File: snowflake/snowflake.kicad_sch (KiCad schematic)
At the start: 19 parts, among them SW1 SK-12E12-G040, U1 RGB, U2 RGB, U25 TPS61022, U3 RGB, U4 RGB

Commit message: 2/6 branches
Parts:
- added C10, C11, C12, C13, C14, C15, C16, C17, C18, C19, C20, C21, C22, C23, C24, C5, C6, C7, C8, C9: 100nF, C_0603_1608Metric, symbol Device:C
- added U10, U11, U12, U13, U14, U15, U16, U17, U18, U19, U20, U21, U22, U23, U24, U5, U6, U7, U8, U9: RGB, easyeda2kicad:LED-SMD_4P-L5.0-W5.0-TL_WS2812B-B, symbol easyeda2kicad:TZ-5050S2RGB-5V-I4-H1
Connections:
- net +5V: now also C10.2, C11.2, C12.2, C13.2, C14.2, C15.2, C16.2, C17.2, C18.2, C19.2, C20.2, C21.2, C22.2, C23.2, C24.2, C5.2, C6.2, C7.2, C8.2, C9.2, U10.1 (VDD), U11.1 (VDD), U12.1 (VDD), U13.1 (VDD), U14.1 (VDD), U15.1 (VDD), U16.1 (VDD), U17.1 (VDD), U18.1 (VDD), U19.1 (VDD), U20.1 (VDD), U21.1 (VDD), U22.1 (VDD), U23.1 (VDD), U24.1 (VDD), U5.1 (VDD), U6.1 (VDD), U7.1 (VDD), U8.1 (VDD), U9.1 (VDD)
- net GND: now also C10.1, C11.1, C12.1, C13.1, C14.1, C15.1, C16.1, C17.1, C18.1, C19.1, C20.1, C21.1, C22.1, C23.1, C24.1, C5.1, C6.1, C7.1, C8.1, C9.1, U10.3 (GND), U11.3 (GND), U12.3 (GND), U13.3 (GND), U14.3 (GND), U15.3 (GND), U16.3 (GND), U17.3 (GND), U18.3 (GND), U19.3 (GND), U20.3 (GND), U21.3 (GND), U22.3 (GND), U23.3 (GND), U24.3 (GND), U5.3 (GND), U6.3 (GND), U7.3 (GND), U8.3 (GND), U9.3 (GND)
- net at U4.2 (DOU): now also U5.4 (DIN)
- new net: U5.2 (DOU), U6.4 (DIN)
- new net: U15.2 (DOU), U16.4 (DIN)
- new net: U14.2 (DOU), U15.4 (DIN)
- new net: U10.4 (DIN), U9.2 (DOU)
- new net: U8.2 (DOU), U9.4 (DIN)
- new net: U22.2 (DOU), U23.4 (DIN)
- new net: U21.2 (DOU), U22.4 (DIN)
- new net: U11.2 (DOU), U12.4 (DIN)
- new net: U10.2 (DOU), U11.4 (DIN)
- new net: U18.2 (DOU), U19.4 (DIN)
- new net: U17.2 (DOU), U18.4 (DIN)
- new net: U23.2 (DOU), U24.4 (DIN)
- new net: U7.2 (DOU), U8.4 (DIN)
- new net: U16.2 (DOU), U17.4 (DIN)
- new net: U13.2 (DOU), U14.4 (DIN)
- new net: U12.2 (DOU), U13.4 (DIN)
- new net: U19.2 (DOU), U20.4 (DIN)
- new net: U6.2 (DOU), U7.4 (DIN)
- new net: U20.2 (DOU), U21.4 (DIN)

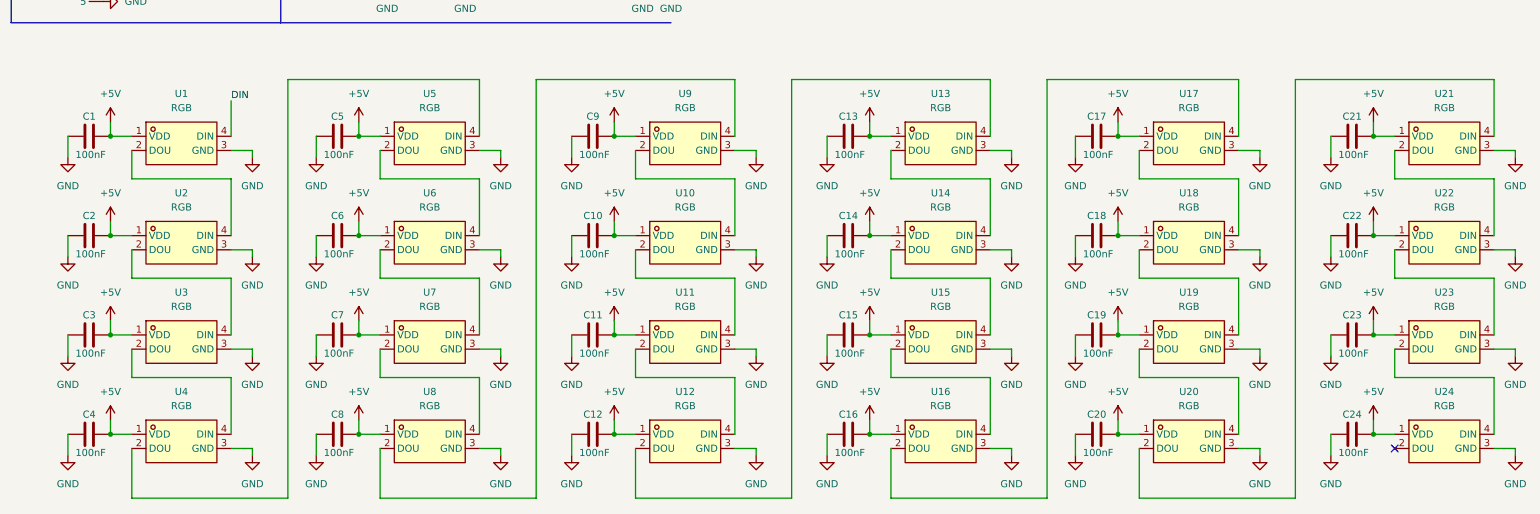
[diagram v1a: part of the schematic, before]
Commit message: Add JLCPCB Part Numbers
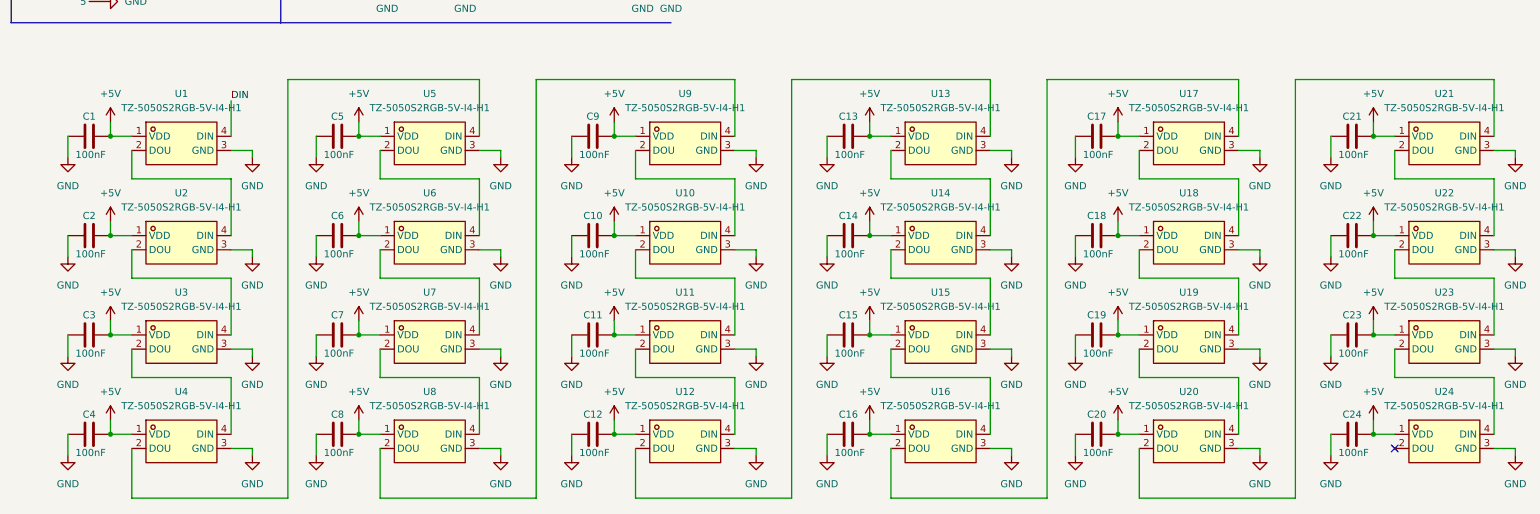
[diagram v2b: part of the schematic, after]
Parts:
- C0: LCSC Part (none) -> C36911391
- C1, C10, C11, C12, C13, C14, C15, C16, C17, C18, C19, C2, C20, C21, C22, C23, C24, C3, C4, C5, C6, C7, C8, C9: footprint C_0603_1608Metric -> Capacitor_SMD:C_0603_1608Metric; LCSC Part (none) -> C36911391
- C25, C26: LCSC Part (none) -> C20416425
- C27: LCSC Part (none) -> C6119842
- R1: LCSC Part (none) -> C5159692
- R2: LCSC Part (none) -> C49652939
- U1, U10, U11, U12, U13, U14, U15, U16, U17, U18, U19, U2, U20, U21, U22, U23, U24, U3, U4, U5, U6, U7, U8, U9: value RGB -> TZ-5050S2RGB-5V-I4-H1
- U25: LCSC Part (none) -> C915088

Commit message: Submitted for cost estimate from JLCPCB
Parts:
- BAT1: LCSC (none) -> C254917; LCSC Part C254917 -> (none)
- C0, C1, C10, C11, C12, C13, C14, C15, C16, C17, C18, C19, C2, C20, C21, C22, C23, C24, C3, C4, C5, C6, C7, C8, C9: LCSC (none) -> C36911391; LCSC Part C36911391 -> (none)
- C25, C26: LCSC (none) -> C20416425; LCSC Part C20416425 -> (none)
- C27: LCSC (none) -> C6119842; LCSC Part C6119842 -> (none)
- L1: LCSC (none) -> C5179444; LCSC Part C5179444 -> (none)
- MCU1: LCSC (none) -> C5346354; LCSC Part C5346354 -> (none)
- R1: LCSC (none) -> C5159692; LCSC Part C5159692 -> (none)
- R2: LCSC (none) -> C49652939; LCSC Part C49652939 -> (none)
- SW1: LCSC (none) -> C22448007; LCSC Part C22448007 -> (none)
- U1, U10, U11, U12, U13, U14, U15, U16, U17, U18, U19, U2, U20, U21, U22, U23, U24, U3, U4, U5, U6, U7, U8, U9: LCSC (none) -> C26167850; LCSC Part C26167850 -> (none)
- U25: LCSC (none) -> C915088; LCSC Part C915088 -> (none)
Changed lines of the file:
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@@
 			)
 		)
-		(property "LCSC Part" "C6119842"
+		(property "LCSC" "C6119842"
 			(at 78.74 21.59 90)
 			(effects
@@
 			)
 		)
-		(property "LCSC Part" "C36911391"
+		(property "LCSC" "C36911391"
 			(at 116.84 120.65 90)
 			(effects
@@
 			)
 		)
-		(property "LCSC Part" "C254917"
-			(at 50.8 48.26 0)
+		(property "LCSC" "C254917"
+			(at 50.8 36.83 0)
 			(effects
 				(font
@@
 			)
 		)
-		(property "LCSC Part" "C36911391"
+		(property "LCSC" "C36911391"
 			(at 162.56 102.87 90)
 			(effects
@@
 			)
 		)
-		(property "LCSC Part" "C26167850"
-			(at 87.63 80.01 0)
+		(property "LCSC" "C26167850"
+			(at 87.63 68.58 0)
 			(effects
 				(font
@@
 			)
 		)
-		(property "LCSC Part" "C36911391"
+		(property "LCSC" "C36911391"
 			(at 116.84 102.87 90)
 			(effects
@@
 			)
 		)
-		(property "LCSC Part" "C36911391"
+		(property "LCSC" "C36911391"
 			(at 26.67 85.09 90)
 			(effects
@@
 			)
 		)
-		(property "LCSC Part" "C36911391"
+		(property "LCSC" "C36911391"
 			(at 252.73 102.87 90)
 			(effects
@@
 			)
 		)
-		(property "LCSC Part" "C5346354"
-			(at 60.96 176.53 0)
+		(property "LCSC" "C5346354"
+			(at 60.96 162.56 0)
 			(effects
 				(font
@@
 			)
 		)
-		(property "LCSC Part" "C915088"
+		(property "LCSC" "C915088"
 			(at 93.98 31.75 0)
 			(effects
@@
 			)
 		)
-		(property "LCSC Part" "C36911391"
+		(property "LCSC" "C36911391"
 			(at 26.67 120.65 90)
 			(effects
@@
 			)
 		)
-		(property "LCSC Part" "C26167850"
-			(at 179.07 115.57 0)
+		(property "LCSC" "C26167850"
+			(at 179.07 104.14 0)
 			(effects
 				(font
@@
 			)
 		)
-		(property "LCSC Part" "C36911391"
+		(property "LCSC" "C36911391"
 			(at 252.73 85.09 90)
 			(effects
@@
 			)
 		)
-		(property "LCSC Part" "C36911391"
+		(property "LCSC" "C36911391"
 			(at 71.12 85.09 90)
 			(effects
@@
 			)
 		)
-		(property "LCSC Part" "C36911391"
+		(property "LCSC" "C36911391"
 			(at 207.01 120.65 90)
 			(effects
@@
 			)
 		)
-		(property "LCSC Part" "C36911391"
+		(property "LCSC" "C36911391"
 			(at 252.73 120.65 90)
 			(effects
@@
 			)
 		)
-		(property "LCSC Part" "C26167850"
-			(at 133.35 80.01 0)
+		(property "LCSC" "C26167850"
+			(at 133.35 68.58 0)
 			(effects
 				(font
@@
 			)
 		)
-		(property "LCSC Part" "C36911391"
+		(property "LCSC" "C36911391"
 			(at 162.56 67.31 90)
 			(effects
@@
 			)
 		)
-		(property "LCSC Part" "C5159692"
+		(property "LCSC" "C5159692"
 			(at 113.03 31.75 90)
 			(effects
@@
 			)
 		)
-		(property "LCSC Part" "C36911391"
+		(property "LCSC" "C36911391"
 			(at 26.67 67.31 90)
 			(effects
@@
 			)
 		)
-		(property "LCSC Part" "C26167850"
-			(at 269.24 97.79 0)
+		(property "LCSC" "C26167850"
+			(at 269.24 86.36 0)
 			(effects
 				(font
@@
 			)
 		)
-		(property "LCSC Part" "C26167850"
-			(at 43.18 97.79 0)
+		(property "LCSC" "C26167850"
+			(at 43.18 86.36 0)
 			(effects
 				(font
@@
 			)
 		)
-		(property "LCSC Part" "C49652939"
+		(property "LCSC" "C49652939"
 			(at 120.65 31.75 90)
 			(effects
@@
 			)
 		)
-		(property "LCSC Part" "C36911391"
+		(property "LCSC" "C36911391"
 			(at 162.56 120.65 90)
 			(effects
@@
 			)
 		)
-		(property "LCSC Part" "C26167850"
-			(at 133.35 115.57 0)
+		(property "LCSC" "C26167850"
+			(at 133.35 104.14 0)
 			(effects
 				(font
@@
 			)
 		)
-		(property "LCSC Part" "C36911391"
+		(property "LCSC" "C36911391"
 			(at 207.01 102.87 90)
 			(effects
@@
 			)
 		)
-		(property "LCSC Part" "C26167850"
-			(at 43.18 133.35 0)
+		(property "LCSC" "C26167850"
+			(at 43.18 121.92 0)
 			(effects
 				(font
@@
 			)
 		)
-		(property "LCSC Part" "C36911391"
+		(property "LCSC" "C36911391"
 			(at 207.01 67.31 90)
 			(effects
@@
 			)
 		)
-		(property "LCSC Part" "C26167850"
-			(at 133.35 97.79 0)
+		(property "LCSC" "C26167850"
+			(at 133.35 86.36 0)
 			(effects
 				(font
@@
 			)
 		)
-		(property "LCSC Part" "C22448007"
-			(at 39.37 38.1 0)
+		(property "LCSC" "C22448007"
+			(at 24.13 38.1 90)
 			(effects
 				(font
@@
 			)
 		)
-		(property "LCSC Part" "C5179444"
-			(at 93.98 31.75 0)
+		(property "LCSC" "C5179444"
+			(at 93.98 21.59 0)
 			(effects
 				(font
@@
 			)
 		)
-		(property "LCSC Part" "C26167850"
-			(at 223.52 97.79 0)
+		(property "LCSC" "C26167850"
+			(at 223.52 86.36 0)
 			(effects
 				(font
@@
 			)
 		)
-		(property "LCSC Part" "C26167850"
-			(at 43.18 115.57 0)
+		(property "LCSC" "C26167850"
+			(at 43.18 104.14 0)
 			(effects
 				(font
@@
 			)
 		)
-		(property "LCSC Part" "C26167850"
-			(at 269.24 133.35 0)
+		(property "LCSC" "C26167850"
+			(at 269.24 121.92 0)
 			(effects
 				(font
@@
 			)
 		)
-		(property "LCSC Part" "C26167850"
-			(at 87.63 133.35 0)
+		(property "LCSC" "C26167850"
+			(at 87.63 121.92 0)
 			(effects
 				(font
@@
 			)
 		)
-		(property "LCSC Part" "C26167850"
-			(at 223.52 80.01 0)
+		(property "LCSC" "C26167850"
+			(at 223.52 68.58 0)
 			(effects
 				(font
@@
 			)
 		)
-		(property "LCSC Part" "C26167850"
-			(at 269.24 115.57 0)
+		(property "LCSC" "C26167850"
+			(at 269.24 104.14 0)
 			(effects
 				(font
@@
 			)
 		)
-		(property "LCSC Part" "C20416425"
+		(property "LCSC" "C20416425"
 			(at 116.84 17.78 90)
 			(effects
@@
 			)
 		)
-		(property "LCSC Part" "C36911391"
+		(property "LCSC" "C36911391"
 			(at 71.12 67.31 90)
 			(effects
@@
 			)
 		)
-		(property "LCSC Part" "C36911391"
+		(property "LCSC" "C36911391"
 			(at 116.84 67.31 90)
 			(effects
@@
 			)
 		)
-		(property "LCSC Part" "C36911391"
+		(property "LCSC" "C36911391"
 			(at 162.56 85.09 90)
 			(effects
@@
 			)
 		)
-		(property "LCSC Part" "C26167850"
-			(at 179.07 80.01 0)
+		(property "LCSC" "C26167850"
+			(at 179.07 68.58 0)
 			(effects
 				(font
@@
 			)
 		)
-		(property "LCSC Part" "C36911391"
+		(property "LCSC" "C36911391"
 			(at 44.45 175.26 0)
 			(effects
@@
 			)
 		)
-		(property "LCSC Part" "C26167850"
-			(at 133.35 133.35 0)
+		(property "LCSC" "C26167850"
+			(at 133.35 121.92 0)
 			(effects
 				(font
@@
 			)
 		)
-		(property "LCSC Part" "C36911391"
+		(property "LCSC" "C36911391"
 			(at 71.12 120.65 90)
 			(effects
@@
 			)
 		)
-		(property "LCSC Part" "C26167850"
-			(at 179.07 97.79 0)
+		(property "LCSC" "C26167850"
+			(at 179.07 86.36 0)
 			(effects
 				(font
@@
 			)
 		)
-		(property "LCSC Part" "C26167850"
-			(at 223.52 115.57 0)
+		(property "LCSC" "C26167850"
+			(at 223.52 104.14 0)
 			(effects
 				(font
@@
 			)
 		)
-		(property "LCSC Part" "C26167850"
-			(at 87.63 115.57 0)
+		(property "LCSC" "C26167850"
+			(at 87.63 104.14 0)
 			(effects
 				(font
@@
 			)
 		)
-		(property "LCSC Part" "C26167850"
-			(at 269.24 80.01 0)
+		(property "LCSC" "C26167850"
+			(at 269.24 68.58 0)
 			(effects
 				(font
@@
 			)
 		)
-		(property "LCSC Part" "C36911391"
+		(property "LCSC" "C36911391"
 			(at 26.67 102.87 90)
 			(effects
@@
 			)
 		)
-		(property "LCSC Part" "C20416425"
+		(property "LCSC" "C20416425"
 			(at 116.84 22.86 90)
 			(effects
@@
 			)
 		)
-		(property "LCSC Part" "C26167850"
-			(at 223.52 133.35 0)
+		(property "LCSC" "C26167850"
+			(at 223.52 121.92 0)
 			(effects
 				(font
@@
 			)
 		)
-		(property "LCSC Part" "C36911391"
+		(property "LCSC" "C36911391"
 			(at 207.01 85.09 90)
 			(effects
@@
 			)
 		)
-		(property "LCSC Part" "C26167850"
-			(at 179.07 133.35 0)
+		(property "LCSC" "C26167850"
+			(at 179.07 121.92 0)
 			(effects
 				(font
@@
 			)
 		)
-		(property "LCSC Part" "C36911391"
+		(property "LCSC" "C36911391"
 			(at 71.12 102.87 90)
 			(effects
@@
 			)
 		)
-		(property "LCSC Part" "C26167850"
-			(at 87.63 97.79 0)
+		(property "LCSC" "C26167850"
+			(at 87.63 86.36 0)
 			(effects
 				(font
@@
 			)
 		)
-		(property "LCSC Part" "C26167850"
-			(at 43.18 80.01 0)
+		(property "LCSC" "C26167850"
+			(at 43.18 68.58 0)
 			(effects
 				(font
@@
 			)
 		)
-		(property "LCSC Part" "C36911391"
+		(property "LCSC" "C36911391"
 			(at 116.84 85.09 90)
 			(effects
@@
 			)
 		)
-		(property "LCSC Part" "C36911391"
+		(property "LCSC" "C36911391"
 			(at 252.73 67.31 90)
 			(effects

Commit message: The nets are happy again
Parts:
- removed BAT1: 2468, easyeda2kicad:BAT-TH_2P-L53.0-W24.6-P12.70_2468, symbol easyeda2kicad:2468
- added BAT1: 2462, easyeda2kicad:BAT-TH_2P-P14.50_2462, symbol easyeda2kicad:2462
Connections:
- net BAT+: now also BAT1.2 (+)
- net GND: now also BAT1.1 (-)

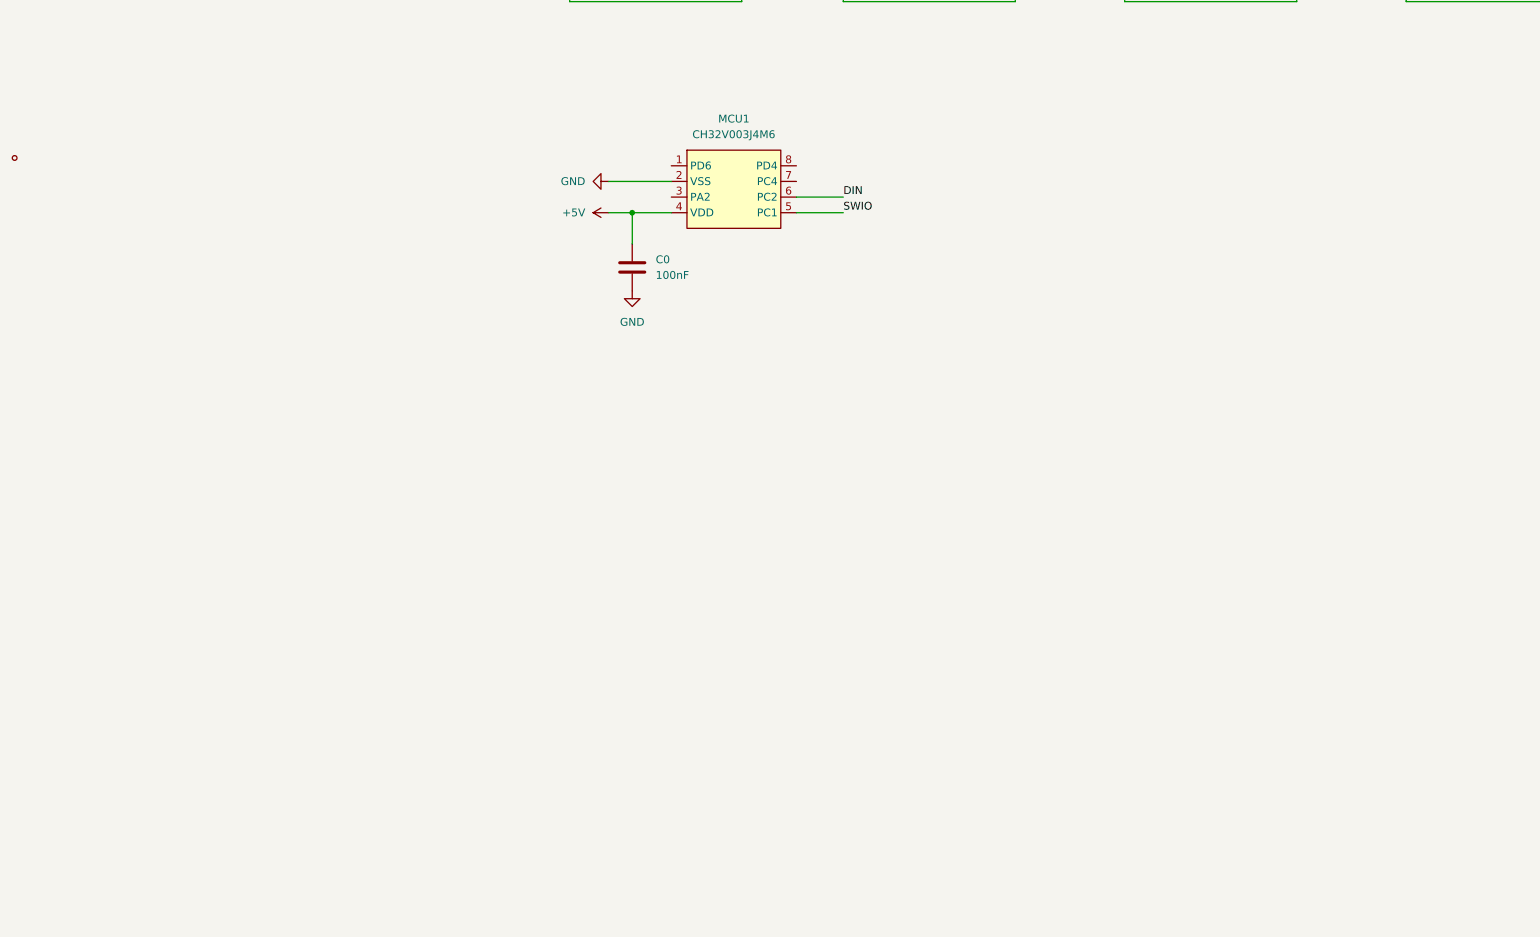
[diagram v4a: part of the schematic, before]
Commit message: Use zones instead of traces for +5V
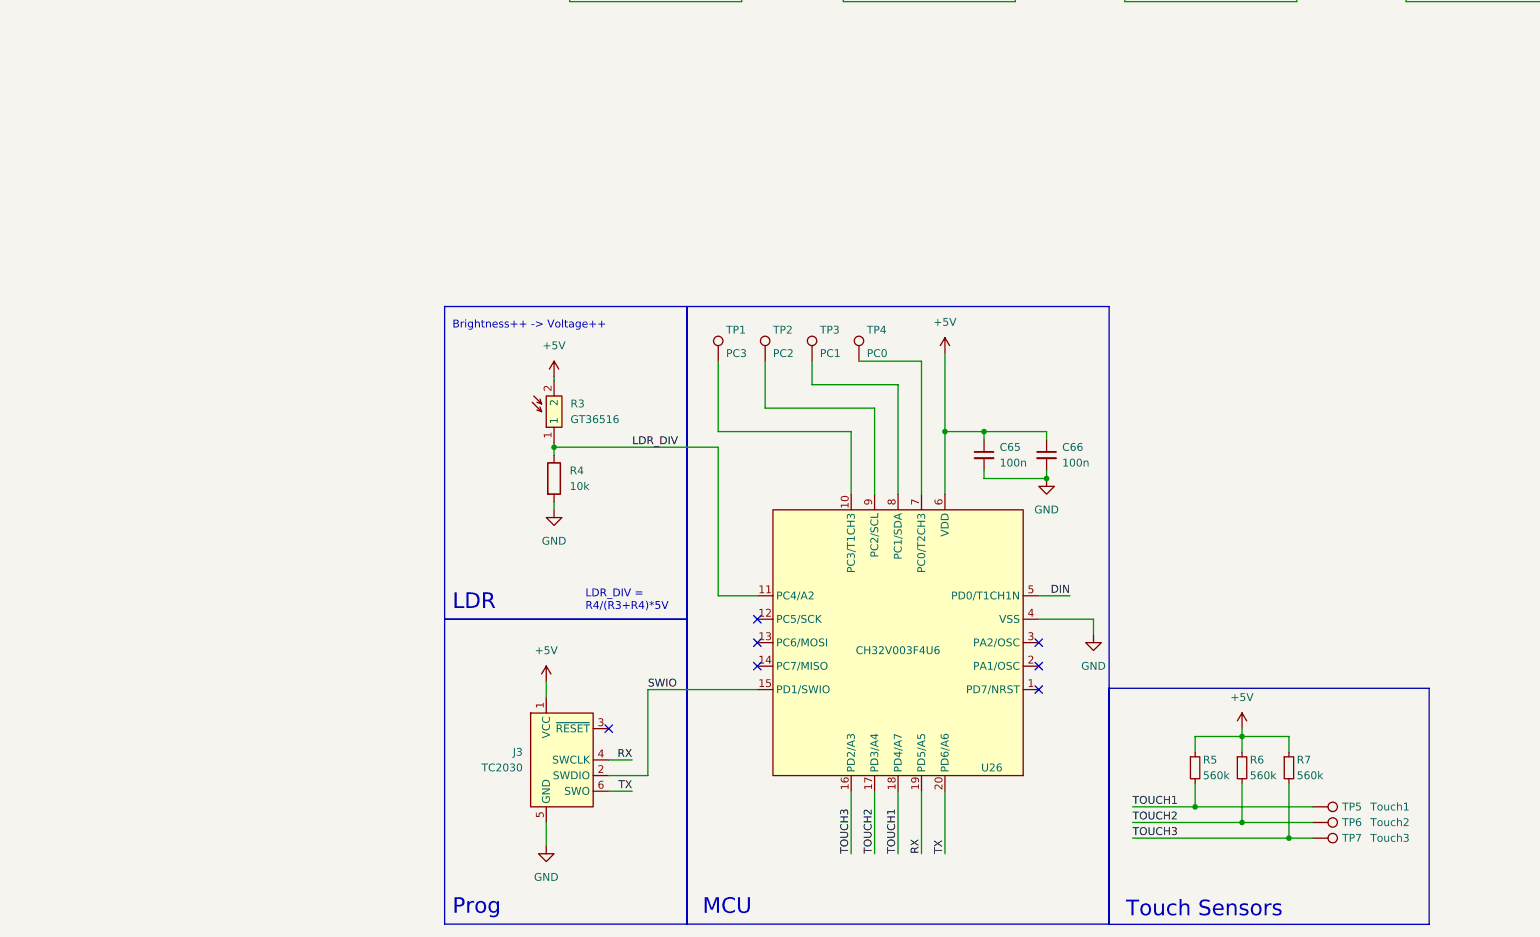
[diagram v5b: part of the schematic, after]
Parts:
- removed C0: 100nF, Capacitor_SMD:C_0603_1608Metric, symbol Device:C
- removed MCU1: CH32V003J4M6, easyeda2kicad:SOP-8_L4.9-W3.8-P1.27-LS6.0-BL, symbol easyeda2kicad:CH32V003J4M6_C5346354
- added C65, C66: 100n, Capacitor_SMD:C_0402_1005Metric, symbol Device:C_Small
- added J3: TC2030, Connector:Tag-Connect_TC2030-IDC-NL_2x03_P1.27mm_Vertical, symbol Connector:Conn_ARM_SWD_TagConnect_TC2030-NL
- added R3: GT36516, easyeda2kicad:RES-SMD_L3.6-W2.4, symbol easyeda2kicad:GT36516
- added R4: 10k, Resistor_SMD:R_0603_1608Metric, symbol Device:R
- added R5, R6, R7: 560k, Resistor_SMD:R_0603_1608Metric, symbol Device:R_Small
- added TP1: PC3, TestPoint:TestPoint_Pad_D2.0mm, symbol Connector:TestPoint
- added TP2: PC2, TestPoint:TestPoint_Pad_D2.0mm, symbol Connector:TestPoint
- added TP3: PC1, TestPoint:TestPoint_Pad_D2.0mm, symbol Connector:TestPoint
- added TP4: PC0, TestPoint:TestPoint_Pad_D2.0mm, symbol Connector:TestPoint
- added TP5: Touch1, TestPoint:TestPoint_Pad_D2.0mm, symbol Connector:TestPoint
- added TP6: Touch2, TestPoint:TestPoint_Pad_D2.0mm, symbol Connector:TestPoint
- added TP7: Touch3, TestPoint:TestPoint_Pad_D2.0mm, symbol Connector:TestPoint
- added U26: CH32V003F4U6, Package_DFN_QFN:QFN-20-1EP_3x3mm_P0.4mm_EP1.65x1.65mm, symbol Back-lib:CH32V003F4U6
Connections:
- net +5V: now also C65.1, C66.1, J3.1 (VCC), R3.2, R5.1, R6.1, R7.1, U26.6 (VDD)
- net DIN: now also U26.5 (PD0/T1CH1N)
- net GND: now also C65.2, C66.2, J3.5 (GND), R4.2, U26.21 (VSS), U26.4 (VSS)
- net SWIO: now also J3.2 (SWDIO), U26.15 (PD1/SWIO)
- new net: TP2.1, U26.9 (PC2/SCL)
- new net: TP1.1, U26.10 (PC3/T1CH3)
- new net: TP4.1, U26.7 (PC0/T2CH3)
- new net: TP3.1, U26.8 (PC1/SDA)
- new net LDR_DIV: R3.1, R4.1, U26.11 (PC4/A2)
- new net RX: J3.4 (SWCLK), U26.19 (PD5/A5)
- new net TOUCH1: R5.2, TP5.1, U26.18 (PD4/A7)
- new net TOUCH2: R6.2, TP6.1, U26.17 (PD3/A4)
- new net TOUCH3: R7.2, TP7.1, U26.16 (PD2/A3)
- new net TX: J3.6 (SWO), U26.20 (PD6/A6)
- no-connect marks 2 -> 9
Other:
- note added: "Brightness++ -> Voltage++"
- note added: "LDR"
- note added: "LDR_DIV = R4/(R3+R4)*5V"
- note added: "MCU"
- note added: "Prog"
- note added: "Touch Sensors"
